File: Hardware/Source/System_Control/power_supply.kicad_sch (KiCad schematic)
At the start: 25 parts, among them J1 POWER_CONN

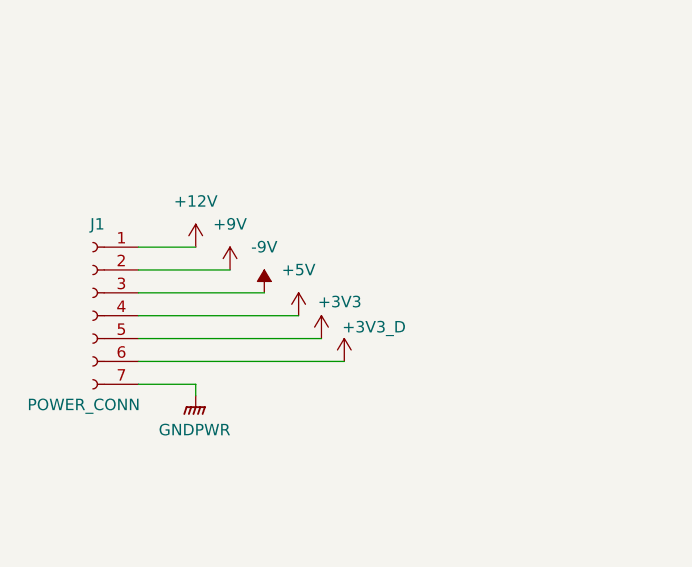
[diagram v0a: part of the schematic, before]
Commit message: schematic: update connector charger board F4
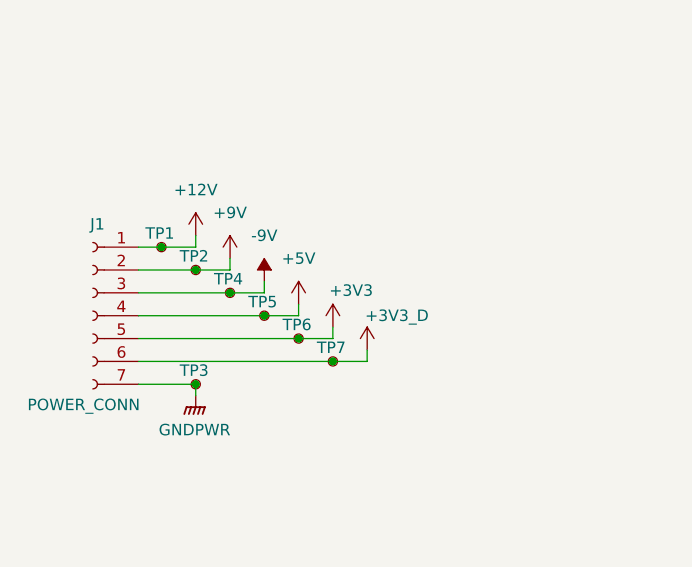
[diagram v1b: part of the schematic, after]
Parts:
- added TP1, TP2, TP3, TP4, TP5, TP6, TP7: TestPoint_Small, TestPoint:TestPoint_Pad_D1.0mm, symbol Connector:TestPoint_Small
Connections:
- net +12V: now also TP1.1
- net +3V3: now also TP6.1
- net +3V3_D: now also TP7.1
- net +5V: now also TP5.1
- net +9V: now also TP2.1
- net -9V: now also TP4.1
- net GNDA: now also TP3.1

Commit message: pcb,lib,sche: PFC, lib: update pcb PFC, lib
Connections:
- net +12V: now also J1.7 (Pin_7); no longer J1.1 (Pin_1)
- net +3V3: now also J1.3 (Pin_3); no longer J1.5 (Pin_5)
- net +3V3_D: now also J1.2 (Pin_2); no longer J1.6 (Pin_6)
- net +9V: now also J1.6 (Pin_6); no longer J1.2 (Pin_2)
- net -9V: now also J1.5 (Pin_5); no longer J1.3 (Pin_3)
- net GNDA: now also J1.1 (Pin_1); no longer J1.7 (Pin_7)
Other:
- moved on the sheet: J1
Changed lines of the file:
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@@
 	(symbol
 		(lib_id "Connector:Conn_01x07_Socket")
-		(at 77.47 81.28 0)
-		(mirror y)
+		(at 77.47 81.28 180)
 		(unit 1)
 		(exclude_from_sim no)
@@
 		(dnp no)
 		(property "Reference" "J1"
-			(at 77.978 71.12 0)
+			(at 77.47 71.628 0)
 			(effects
 				(font
@@
 		)
 		(property "Value" "POWER_CONN"
-			(at 76.454 91.186 0)
+			(at 77.47 91.44 0)
 			(effects
 				(font

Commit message: pull
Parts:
- removed C2: 10uF/35V, charge_battery_footprint_lib:Tan_Cap_C, symbol charge_battery_sym_lib:Cap_Tantalum_10uF_35V
- removed C4: 1uF/35V, charge_battery_footprint_lib:Tan_Cap_A, symbol charge_battery_sym_lib:Cap_Tantalum_1uF_35V
- removed J1: POWER_CONN, Connector_Phoenix_MC:PhoenixContact_MC_1,5_7-G-3.81_1x07_P3.81mm_Horizontal, symbol Connector:Conn_01x07_Socket
- removed TP1: TestPoint_Small, TestPoint:TestPoint_Pad_D1.0mm, symbol Connector:TestPoint_Small
- added J1: POWER_CONN, Connector_Phoenix_MC:PhoenixContact_MC_1,5_6-G-3.81_1x06_P3.81mm_Horizontal, symbol Connector:Conn_01x06_Socket
- renumbered C11 to C10, C3 to C2, C6 to C3, C5 to C4, C8 to C5, C7 to C6, C10 to C7, C9 to C8, C12 to C9, TP2 to TP1, TP3 to TP2, TP4 to TP3, TP5 to TP4, TP6 to TP5, TP7 to TP6
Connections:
- net +3V3: now also J1.3 (Pin_3)
- net +3V3_D: now also J1.2 (Pin_2)
- net +5V: now also J1.4 (Pin_4)
- net +9V: now also J1.6 (Pin_6)
- net -9V: now also J1.5 (Pin_5)
- net GNDA: now also J1.1 (Pin_1)
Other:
- moved on the sheet: C10, C3, C5, C7, C8, C9

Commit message: check
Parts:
- removed D1: LED_0805, charge_battery_footprint_lib:LED_0805, symbol charge_battery_sym_lib:LED_0805
- removed R1: 1K/1%/1_10W, charge_battery_footprint_lib:Res_0603, symbol charge_battery_sym_lib:Res_1K_0603_1%
- added H1: MountingHole, MountingHole:MountingHole_3.2mm_M3_ISO7380_Pad_TopBottom, symbol Mechanical:MountingHole
- renumbered D2 to D1, D3 to D2, D4 to D3, D5 to D4, D6 to D5, R2 to R1, R3 to R2, R4 to R3, R5 to R4, R6 to R5
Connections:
- net +3V3: now also J1.5 (Pin_5), TP3.1; no longer J1.3 (Pin_3), TP5.1
- net +3V3_D: now also J1.4 (Pin_4), TP4.1; no longer J1.2 (Pin_2), TP6.1
- net +5V: now also J1.6 (Pin_6), TP1.1; no longer J1.4 (Pin_4), TP4.1
- net +9V: now also J1.3 (Pin_3), TP5.1; no longer J1.6 (Pin_6), TP1.1
- net -9V: now also J1.2 (Pin_2), TP6.1; no longer J1.5 (Pin_5), TP3.1

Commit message: check
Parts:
- removed TP2, TP3, TP4, TP5, TP6: TestPoint_Small, TestPoint:TestPoint_Pad_D1.0mm, symbol Connector:TestPoint_Small
- TP1: value TestPoint_Small -> GND
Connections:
- net +5V: no longer TP1.1
- net GNDA: now also TP1.1
- net +3V3_D renamed +3V3_O

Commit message: check
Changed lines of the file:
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@@
 				)
 				(justify left)
+				(hide yes)
 			)
 		)

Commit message: lib:foot, sym: upload opamp iso, led 5
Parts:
- H1: footprint MountingHole:MountingHole_3.2mm_M3_ISO7380_Pad_TopBottom -> MountingHole:MountingHole_3.2mm_M3_Pad_Via
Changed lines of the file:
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@@
 			)
 		)
-		(property "Footprint" "MountingHole:MountingHole_3.2mm_M3_ISO7380_Pad_TopBottom"
+		(property "Footprint" "MountingHole:MountingHole_3.2mm_M3_Pad_Via"
 			(at 124.46 167.64 0)
 			(effects
